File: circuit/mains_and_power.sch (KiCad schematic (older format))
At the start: 25 parts, among them J1 Screw_Terminal_01x10, U1 AQH213A, U2 AQH213A, U3 AQH213A, U4 VTX-214-005-112, U5 TL7660, U6 AOZ1280CI

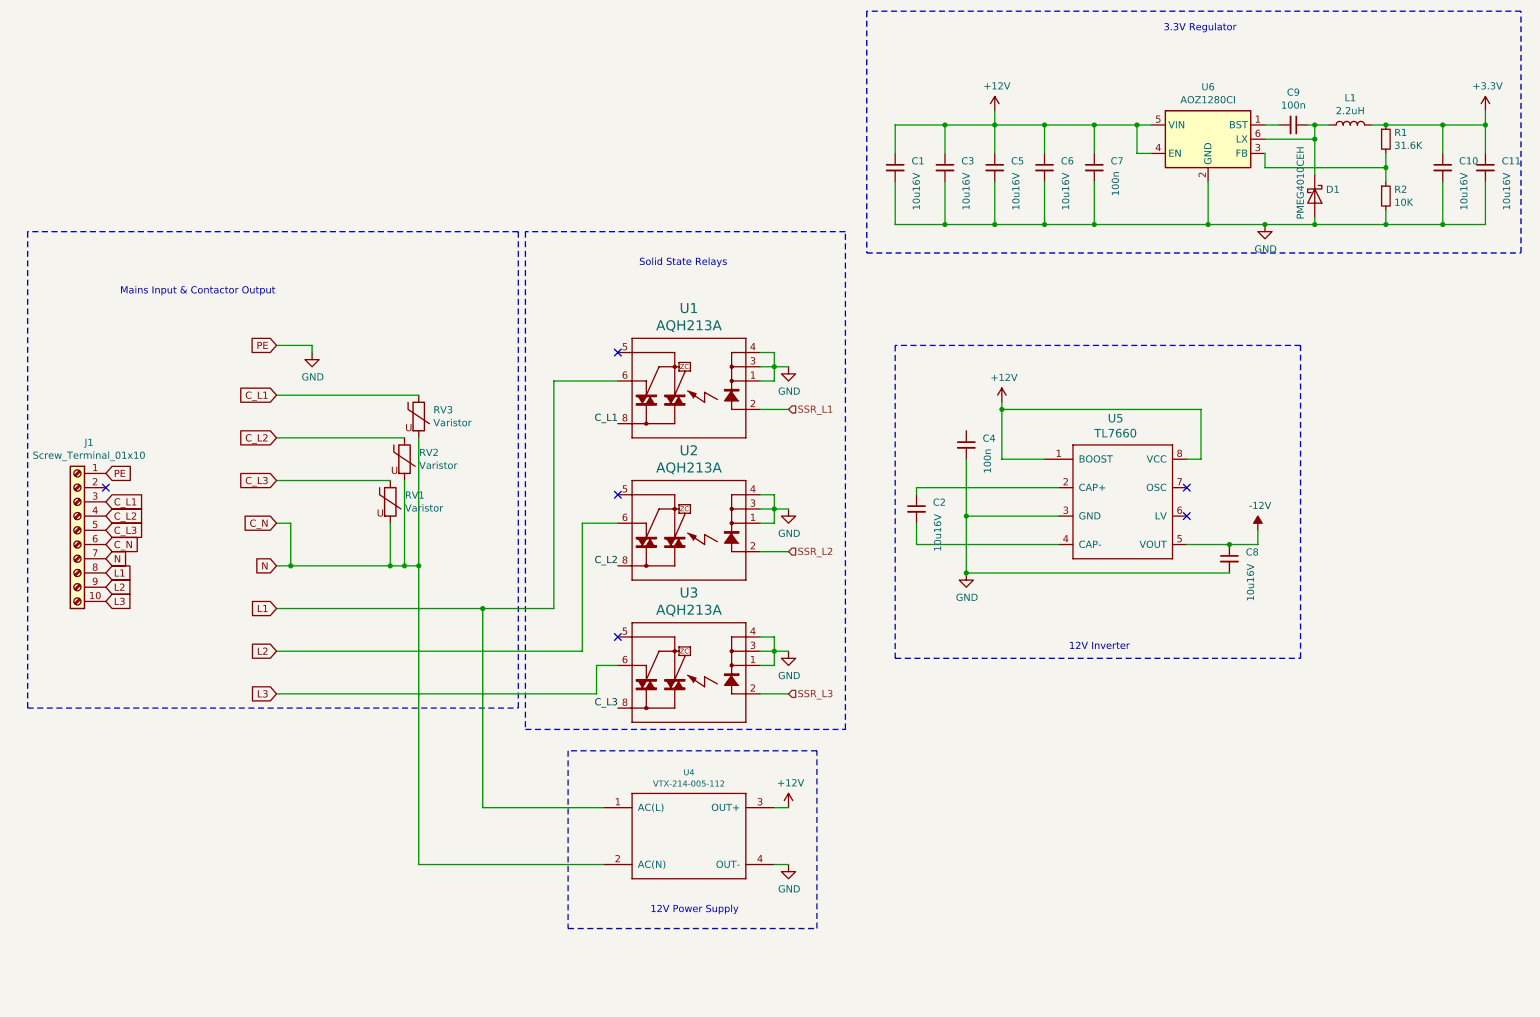
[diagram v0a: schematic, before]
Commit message: Update to rev0.1 of atmevse circuit
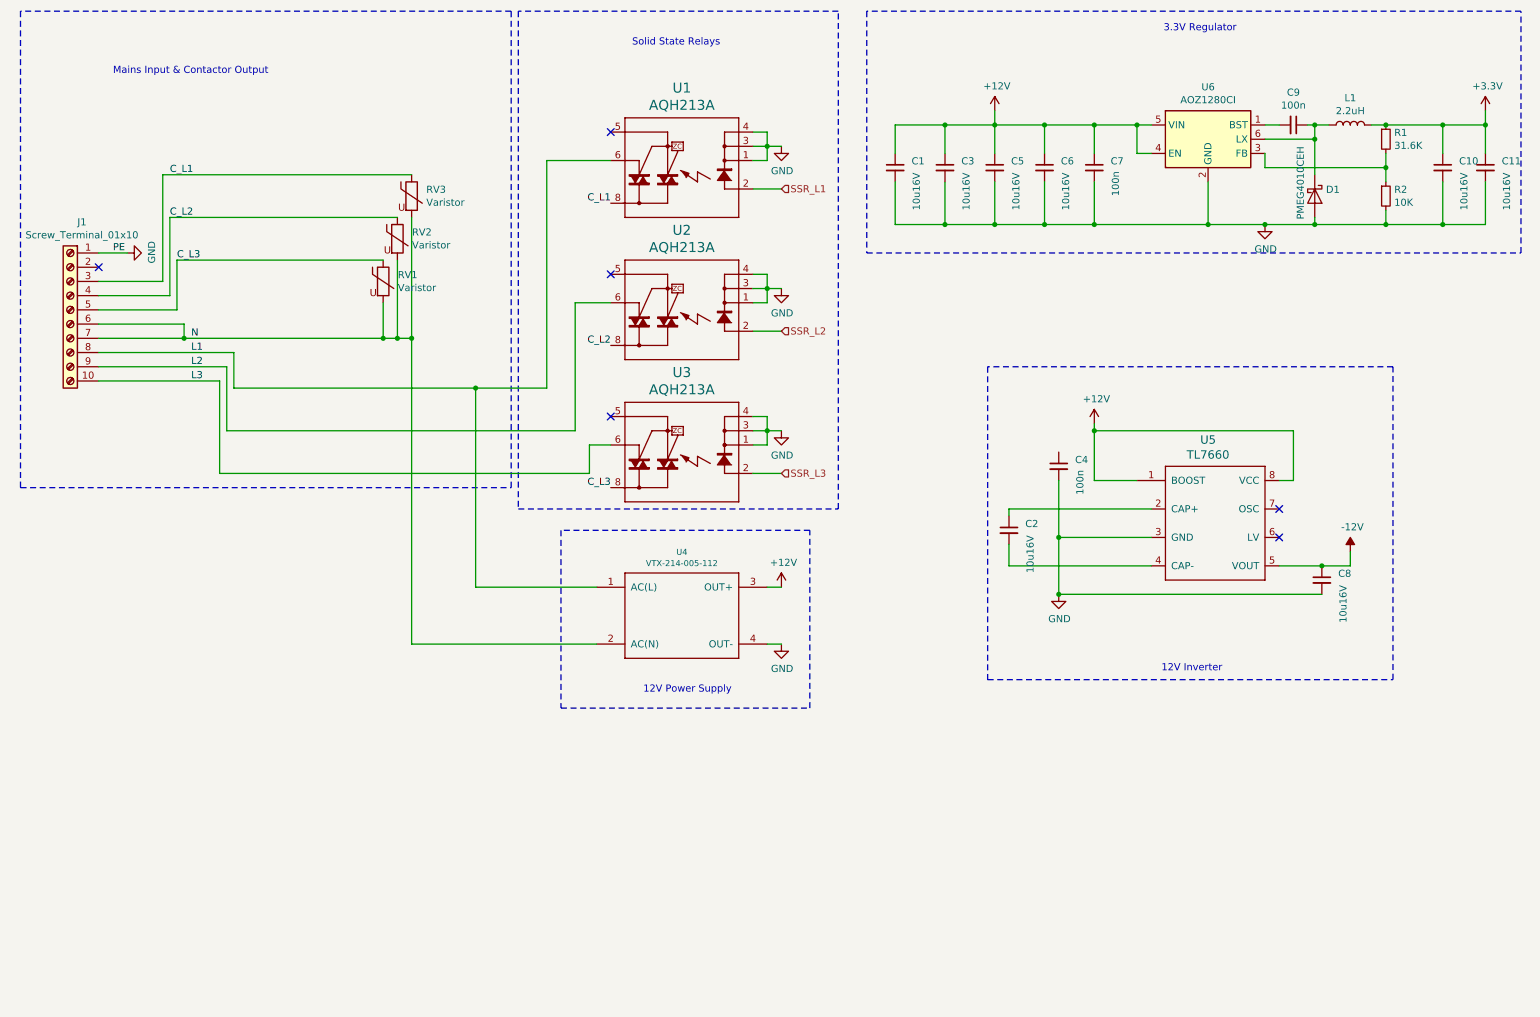
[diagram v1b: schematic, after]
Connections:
- net C_N renamed N
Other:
- moved on the sheet: C2, C4, C8, J1, RV1, RV2, RV3, U1, U2, U3, U4, U5

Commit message: Update schematic to rev0.2
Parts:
- added C21, C22, C23: 100n, symbol Device:C_Small
- added J4, J5, J6: AudioJack3_Tip_Switch, symbol smartevse:AudioJack3_Tip_Switch
- added R25, R26, R27: 22, symbol Device:R_Small
- added R28, R29, R30: 100, symbol Device:R_Small
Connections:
- net labels added: BIAS, CT0, CT1, CT2
- wire segments 129 -> 165
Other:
- note added: "Current Transformer Input Section\n"

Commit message: Update Schematic with Prof. Moor's suggestions
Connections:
- net labels added: L
- net labels removed: L1, L2, L3
- wire segments 165 -> 156
- no-connect marks 6 -> 8
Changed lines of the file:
@@
 Sheet 2 4
 Title ""
-Date "2020-04-10"
-Rev "0.2"
+Date "2020-05-12"
+Rev "0.4"
 Comp ""
 Comment1 "DONE: CT input circuit"
-Comment2 "TODO: verify CT input circuit in sim (maybe rectify signal?)"
-Comment3 ""
+Comment2 "DONE: Edit SSR connections"
+Comment3 "TODO: verify CT input circuit in sim (maybe rectify signal?)"
 Comment4 ""
 $EndDescr
@@
 	5700 2000 5900 2000
 Wire Wire Line
-	4550 4000 4550 3800
-Wire Wire Line
-	4550 3800 4700 3800
-Wire Wire Line
-	4450 3700 4450 2800
-Wire Wire Line
-	4450 2800 4700 2800
-Wire Wire Line
-	4250 3400 4250 1800
-Wire Wire Line
 	4250 1800 4700 1800
 NoConn ~ 4700 1600
@@
 Wire Wire Line
 	3300 5200 4600 5200
-Wire Wire Line
-	3750 4800 4600 4800
-Connection ~ 3750 3400
-Wire Wire Line
-	3750 3400 4250 3400
 Text Label 4700 2100 2    50   ~ 0
 C_L1
@@
 Text Notes 9000 5400 2    50   ~ 0
 12V Inverter\n
-Wire Wire Line
-	3750 3400 3750 4800
 $Comp
 L Connector:Screw_Terminal_01x10 J1
@@
 Wire Wire Line
 	1700 3050 3100 3050
-Wire Wire Line
-	1100 3150 2050 3150
-Wire Wire Line
-	2050 3150 2050 3400
-Wire Wire Line
-	2050 3400 3750 3400
-Text Label 1750 3150 0    50   ~ 0
-L1
-Wire Wire Line
-	1100 3250 2000 3250
-Wire Wire Line
-	2000 3250 2000 3700
-Wire Wire Line
-	2000 3700 4450 3700
-Text Label 1750 3250 0    50   ~ 0
-L2
-Wire Wire Line
-	1100 3350 1950 3350
-Wire Wire Line
-	1950 3350 1950 4000
-Wire Wire Line
-	1950 4000 4550 4000
-Text Label 1750 3350 0    50   ~ 0
-L3
 $Comp
 L power:GND #PWR01
@@
 Text Notes 2650 7600 2    50   ~ 0
 Current Transformer Input Section\n
+Wire Wire Line
+	4250 3800 4700 3800
+Wire Wire Line
+	4250 2800 4700 2800
+Connection ~ 4250 2800
+Wire Wire Line
+	4250 2800 4250 1800
+Wire Wire Line
+	4250 3800 4250 4800
+Connection ~ 4250 3800
+Wire Wire Line
+	4250 4800 4600 4800
+Wire Wire Line
+	4250 2800 4250 3350
+Wire Wire Line
+	1100 3350 4250 3350
+Connection ~ 4250 3350
+Wire Wire Line
+	4250 3350 4250 3800
+Text Label 1700 3350 0    50   ~ 0
+L
+NoConn ~ 1100 3150
+NoConn ~ 1100 3250
 $EndSCHEMATC

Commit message: Update schematic with suggestions
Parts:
- added R? (x2): 10k, symbol Device:R_Small
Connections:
- wire segments 156 -> 161
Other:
- note added: "VDD/2 Bias Voltage for CT input\n"
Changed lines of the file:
@@
 Comment2 "DONE: Edit SSR connections"
 Comment3 "TODO: verify CT input circuit in sim (maybe rectify signal?)"
-Comment4 ""
+Comment4 "DONE: add bias voltage (VDD/2)"
 $EndDescr
 $Comp
@@
 NoConn ~ 1100 3150
 NoConn ~ 1100 3250
+$Comp
+L power:+3.3V #PWR?
+U 1 1 5ED48069
+P 4500 6200
+F 0 "#PWR?" H 4500 6050 50  0001 C CNN
+F 1 "+3.3V" H 4515 6373 50  0000 C CNN
+F 2 "" H 4500 6200 50  0001 C CNN
+F 3 "" H 4500 6200 50  0001 C CNN
+	1    4500 6200
+	1    0    0    -1
+$EndComp
+$Comp
+L power:GND #PWR?
+U 1 1 5ED48B00
+P 4500 6900
+F 0 "#PWR?" H 4500 6650 50  0001 C CNN
+F 1 "GND" H 4505 6727 50  0000 C CNN
+F 2 "" H 4500 6900 50  0001 C CNN
+F 3 "" H 4500 6900 50  0001 C CNN
+	1    4500 6900
+	1    0    0    -1
+$EndComp
+$Comp
+L Device:R_Small R?
+U 1 1 5ED491A0
+P 4500 6700
+F 0 "R?" H 4559 6746 50  0000 L CNN
+F 1 "10k" H 4559 6655 50  0000 L CNN
+F 2 "" H 4500 6700 50  0001 C CNN
+F 3 "~" H 4500 6700 50  0001 C CNN
+	1    4500 6700
+	1    0    0    -1
+$EndComp
+$Comp
+L Device:R_Small R?
+U 1 1 5ED49F5A
+P 4500 6350
+F 0 "R?" H 4559 6396 50  0000 L CNN
+F 1 "10k" H 4559 6305 50  0000 L CNN
+F 2 "" H 4500 6350 50  0001 C CNN
+F 3 "~" H 4500 6350 50  0001 C CNN
+	1    4500 6350
+	1    0    0    -1
+$EndComp
+Wire Wire Line
+	4500 6200 4500 6250
+Wire Wire Line
+	4500 6800 4500 6900
+Wire Wire Line
+	4500 6450 4500 6500
+Wire Wire Line
+	4500 6500 4100 6500
+Connection ~ 4500 6500
+Wire Wire Line
+	4500 6500 4500 6600
+Text Label 4100 6500 0    50   ~ 0
+BIAS
+Wire Notes Line
+	3900 5900 5000 5900
+Wire Notes Line
+	5000 5900 5000 7300
+Wire Notes Line
+	5000 7300 3900 7300
+Wire Notes Line
+	3900 7300 3900 5900
+Text Notes 3850 7400 0    50   ~ 0
+VDD/2 Bias Voltage for CT input\n
 $EndSCHEMATC

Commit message: Edit schematic
Moved CT input to J2
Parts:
- removed C21, C22, C23: 100n, symbol Device:C_Small
- removed J4, J5, J6: AudioJack3_Tip_Switch, symbol smartevse:AudioJack3_Tip_Switch
- removed R25, R26, R27: 22, symbol Device:R_Small
- removed R28, R29, R30: 100, symbol Device:R_Small
- removed R? (x2): 10k, symbol Device:R_Small
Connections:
- net labels removed: BIAS, CT0, CT1, CT2
- wire segments 161 -> 120
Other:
- note removed: "Current Transformer Input Section\n"
- note removed: "VDD/2 Bias Voltage for CT input\n"

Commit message: Add new component data in schematic
Updated components and footprints in schematic
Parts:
- added F?: T1.25A, smartevse-footprints:TE5, symbol smartevse:FuseT1.25
- C1, C10, C11, C2, C3, C5, C6, C8: footprint (none) -> Capacitor_SMD:C_0805_2012Metric_Pad1.15x1.40mm_HandSolder; Part (none) -> Würth Elektronik WCAP-CSGP 885012107014 Keramik-Kondensator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; PartNo (none) -> 1278809; Supplier (none) -> Conrad
- C4, C7, C9: footprint (none) -> Capacitor_SMD:C_0603_1608Metric_Pad1.05x0.95mm_HandSolder; Part (none) -> Kemet C0603C104K3RAC7867+ Keramik-Kondensator SMD 0603 100 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; PartNo (none) -> 1420339; Supplier (none) -> Conrad
- D1: value PMEG4010CEH -> PMEG4010BEA; footprint Diode_SMD:D_SOD-128 -> Diode_SMD:D_SOD-323_HandSoldering; Part (none) -> Nexperia Schottky-Diode - Gleichrichter PMEG4010BEA,135 SOD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; PartNo (none) -> 1111813; Supplier (none) -> Conrad
- J1: symbol Connector:Screw_Terminal_01x10 -> smartevse:Screw_Terminal_01x10
- L1: footprint (none) -> Inductor_SMD:L_1210_3225Metric_Pad1.42x2.65mm_HandSolder; Part (none) -> Würth Elektronik WE-GFH 744764902 HF-Drossel SMD 3225 2.2 µ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; PartNo (none) -> 1385329; Supplier (none) -> Conrad
- R1: value 31.6K -> 31.6k; footprint (none) -> Resistor_SMD:R_0603_1608Metric_Pad1.05x0.95mm_HandSolder; Part (none) -> TRU COMPONENTS TC-0603SAJ0303T5E203 Dickschicht-Widerstand 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; PartNo (none) -> 1584281; Supplier (none) -> Conrad
- R2: value 10K -> 10k; footprint (none) -> Resistor_SMD:R_0603_1608Metric_Pad1.05x0.95mm_HandSolder; Part (none) -> TRU COMPONENTS TC-0603SAF1002T5E203 Dickschicht-Widerstand 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; PartNo (none) -> 1585269; Supplier (none) -> Conrad
- RV1, RV2, RV3: footprint (none) -> Varistor:RV_Disc_D16.5mm_W6.7mm_P7.5mm; symbol Device:Varistor -> smartevse:Varistor; Part (none) -> TDK S14K275 Scheiben-Varistor 430V; PartNo (none) -> 500675; Supplier (none) -> Conrad
- U1, U2, U3: value AQH213A -> AQH3223; symbol smartevse:AQH213A -> smartevse:AQH3223; Part (none) -> Panasonic Halbleiterrelais AQH3223 Sofortschaltend; PartNo (none) -> 504887; Supplier (none) -> Conrad
- U4: value VTX-214-005-112 -> MPM-05-12; symbol smartevse:VTX-214-005-112 -> smartevse:MPM-05-12; Part (none) -> Mean Well MPM-05-12 AC/DC-Printnetzteil 12 V/DC 0.42 A 5 W; PartNo (none) -> 1838042; Supplier (none) -> Conrad
- U5: value TL7660 -> ICL7660; symbol smartevse:TL7660 -> smartevse:ICL7660; Part (none) -> Maxim Integrated ICL7662CBA+ PMIC; PartNo (none) -> 1123919; Supplier (none) -> Conrad
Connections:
- net +12V: now also C4.1
- net L: now also F?.2; no longer U1.6 (DS3), U2.6 (DS3), U3.6 (DS3), U4.1 (AC(L))
- new net: F?.1, U1.6 (DS3), U2.6 (DS3), U3.6 (DS3), U4.1 (AC(L))
